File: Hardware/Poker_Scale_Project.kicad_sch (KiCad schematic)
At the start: 3 parts, among them U1 MCP6241-E/P

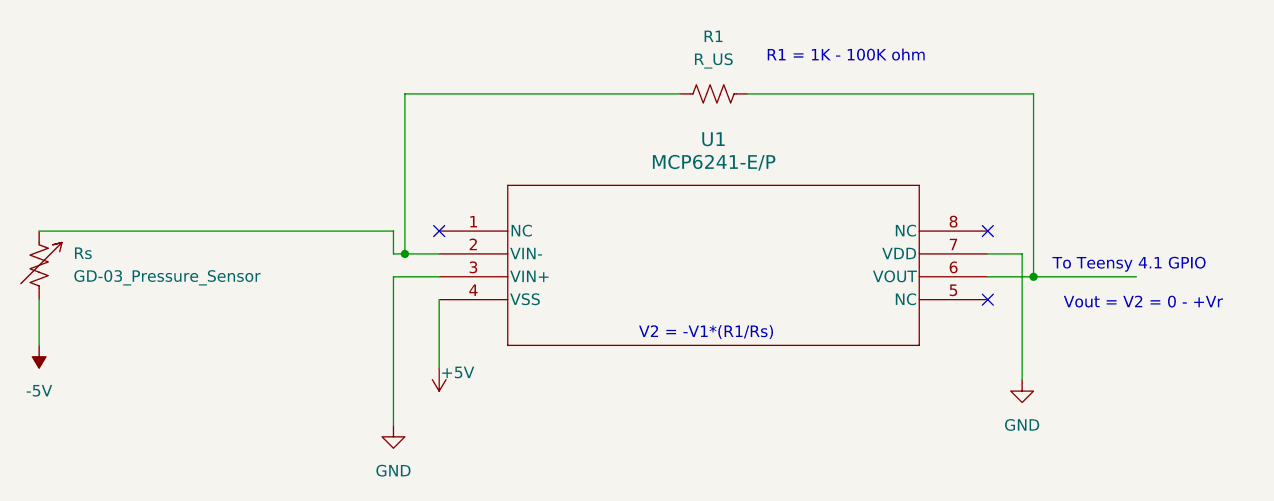
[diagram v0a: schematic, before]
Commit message: fixing Scale circuit, V2 = 0V - 3.3VDC
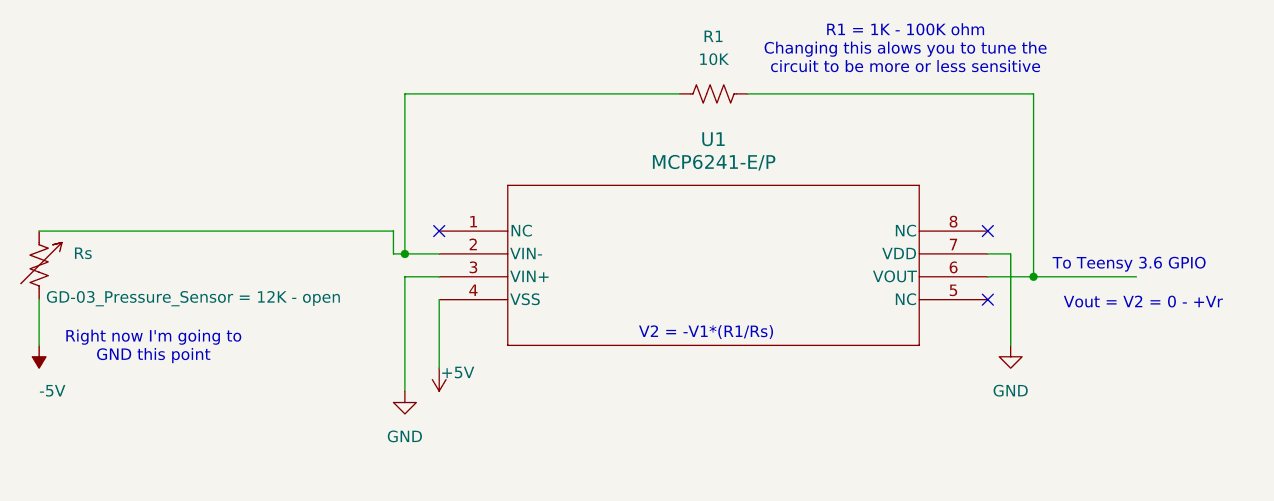
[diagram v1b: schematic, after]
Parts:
- R1: value R_US -> 10K
- Rs: value GD-03_Pressure_Sensor -> GD-03_Pressure_Sensor = 12K - open
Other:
- note added: "R1 = 1K - 100K ohm Changing this alows you to tune the circuit to be more or less sensitive"
- note added: "Right now I'm going to GND this point"
- note added: "To Teensy 3.6 GPIO"
- note removed: "R1 = 1K - 100K ohm"
- note removed: "To Teensy 4.1 GPIO"
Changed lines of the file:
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@@
 	(wire
 		(pts
-			(xy 167.64 101.6) (xy 163.83 101.6)
+			(xy 163.83 101.6) (xy 166.37 101.6)
 		)
 		(stroke
@@
 	(wire
 		(pts
-			(xy 102.87 104.14) (xy 97.79 104.14)
-		)
-		(stroke
-			(width 0)
-			(type default)
-		)
-	)
-	(wire
-		(pts
-			(xy 102.87 106.68) (xy 102.87 114.3)
+			(xy 102.87 114.3) (xy 102.87 106.68)
 		)
 		(stroke
@@
 	(wire
 		(pts
-			(xy 167.64 115.57) (xy 167.64 101.6)
+			(xy 99.06 104.14) (xy 102.87 104.14)
+		)
+		(stroke
+			(width 0)
+			(type default)
+		)
+	)
+	(wire
+		(pts
+			(xy 166.37 111.76) (xy 166.37 101.6)
 		)
 		(stroke
@@
 	(wire
 		(pts
+			(xy 99.06 116.84) (xy 99.06 104.14)
+		)
+		(stroke
+			(width 0)
+			(type default)
+		)
+	)
+	(wire
+		(pts
 			(xy 168.91 104.14) (xy 163.83 104.14)
 		)
@@
 		)
 	)
-	(wire
-		(pts
-			(xy 97.79 104.14) (xy 97.79 120.65)
-		)
-		(stroke
-			(width 0)
-			(type default)
+	(text "Right now I'm going to\nGND this point\n"
+		(exclude_from_sim no)
+		(at 71.12 112.014 0)
+		(effects
+			(font
+				(size 1.27 1.27)
+			)
 		)
 	)
@@
 		)
 	)
-	(text "To Teensy 4.1 GPIO\n"
+	(text "To Teensy 3.6 GPIO\n"
 		(exclude_from_sim no)
 		(at 179.578 102.87 0)
@@
 		)
 	)
-	(text "R1 = 1K - 100K ohm"
-		(exclude_from_sim no)
-		(at 148.082 79.756 0)
+	(text "R1 = 1K - 100K ohm\nChanging this alows you to tune the \ncircuit to be more or less sensitive "
+		(exclude_from_sim no)
+		(at 154.686 78.994 0)
 		(effects
 			(font
 				(size 1.27 1.27)
+			)
+		)
+	)
+	(symbol
+		(lib_id "power:GND")
+		(at 166.37 111.76 0)
+		(unit 1)
+		(exclude_from_sim no)
+		(in_bom yes)
+		(on_board yes)
+		(dnp no)
+		(fields_autoplaced yes)
+		(property "Reference" "#PWR03"
+			(at 166.37 118.11 0)
+			(effects
+				(font
+					(size 1.27 1.27)
+				)
+				(hide yes)
+			)
+		)
+		(property "Value" "GND"
+			(at 166.37 116.84 0)
+			(effects
+				(font
+					(size 1.27 1.27)
+				)
+			)
+		)
+		(property "Footprint" ""
+			(at 166.37 111.76 0)
+			(effects
+				(font
+					(size 1.27 1.27)
+				)
+				(hide yes)
+			)
+		)
+		(property "Datasheet" ""
+			(at 166.37 111.76 0)
+			(effects
+				(font
+					(size 1.27 1.27)
+				)
+				(hide yes)
+			)
+		)
+		(property "Description" "Power symbol creates a global label with name \"GND\" , ground"
+			(at 166.37 111.76 0)
+			(effects
+				(font
+					(size 1.27 1.27)
+				)
+				(hide yes)
+			)
+		)
+		(pin "1"
+		)
+		(instances
+			(project "Poker_Scale_Project"
+				(path "/dad62ed6-c118-47a2-9ae4-23cb6e0602fb"
+					(reference "#PWR03")
+					(unit 1)
+				)
 			)
 		)
@@
 		(on_board yes)
 		(dnp no)
-		(fields_autoplaced yes)
 		(property "Reference" "Rs"
 			(at 62.23 101.5618 0)
@@
 			)
 		)
-		(property "Value" "GD-03_Pressure_Sensor"
-			(at 62.23 104.1018 0)
+		(property "Value" "GD-03_Pressure_Sensor = 12K - open"
+			(at 59.182 106.426 0)
 			(effects
 				(font
@@
 	(symbol
 		(lib_id "power:GND")
-		(at 97.79 120.65 0)
-		(unit 1)
-		(exclude_from_sim no)
-		(in_bom yes)
-		(on_board yes)
-		(dnp no)
-		(fields_autoplaced yes)
-		(property "Reference" "#PWR01"
-			(at 97.79 127 0)
-			(effects
-				(font
-					(size 1.27 1.27)
-				)
-				(hide yes)
-			)
-		)
-		(property "Value" "GND"
-			(at 97.79 125.73 0)
-			(effects
-				(font
-					(size 1.27 1.27)
-				)
-			)
-		)
-		(property "Footprint" ""
-			(at 97.79 120.65 0)
-			(effects
-				(font
-					(size 1.27 1.27)
-				)
-				(hide yes)
-			)
-		)
-		(property "Datasheet" ""
-			(at 97.79 120.65 0)
-			(effects
-				(font
-					(size 1.27 1.27)
-				)
-				(hide yes)
-			)
-		)
-		(property "Description" "Power symbol creates a global label with name \"GND\" , ground"
-			(at 97.79 120.65 0)
-			(effects
-				(font
-					(size 1.27 1.27)
-				)
-				(hide yes)
-			)
-		)
-		(pin "1"
-		)
-		(instances
-			(project ""
-				(path "/dad62ed6-c118-47a2-9ae4-23cb6e0602fb"
-					(reference "#PWR01")
-					(unit 1)
-				)
-			)
-		)
-	)
-	(symbol
-		(lib_id "power:GND")
-		(at 167.64 115.57 0)
+		(at 99.06 116.84 0)
 		(unit 1)
 		(exclude_from_sim no)
@@
 		(fields_autoplaced yes)
 		(property "Reference" "#PWR02"
-			(at 167.64 121.92 0)
+			(at 99.06 123.19 0)
 			(effects
 				(font
@@
 		)
 		(property "Value" "GND"
-			(at 167.64 120.65 0)
+			(at 99.06 121.92 0)
 			(effects
 				(font
@@
 		)
 		(property "Footprint" ""
-			(at 167.64 115.57 0)
+			(at 99.06 116.84 0)
 			(effects
 				(font
@@
 		)
 		(property "Datasheet" ""
-			(at 167.64 115.57 0)
+			(at 99.06 116.84 0)
 			(effects
 				(font
@@
 		)
 		(property "Description" "Power symbol creates a global label with name \"GND\" , ground"
-			(at 167.64 115.57 0)
+			(at 99.06 116.84 0)
 			(effects
 				(font
@@
 			)
 		)
-		(property "Value" "R_US"
+		(property "Value" "10K"
 			(at 133.35 80.01 90)
 			(effects
@@
 	)
 	(symbol
+		(lib_id "power:+5V")
+		(at 102.87 114.3 180)
+		(unit 1)
+		(exclude_from_sim no)
+		(in_bom yes)
+		(on_board yes)
+		(dnp no)
+		(property "Reference" "#PWR01"
+			(at 102.87 110.49 0)
+			(effects
+				(font
+					(size 1.27 1.27)
+				)
+				(hide yes)
+			)
+		)
+		(property "Value" "+5V"
+			(at 104.902 114.808 0)
+			(effects
+				(font
+					(size 1.27 1.27)
+				)
+			)
+		)
+		(property "Footprint" ""
+			(at 102.87 114.3 0)
+			(effects
+				(font
+					(size 1.27 1.27)
+				)
+				(hide yes)
+			)
+		)
+		(property "Datasheet" ""
+			(at 102.87 114.3 0)
+			(effects
+				(font
+					(size 1.27 1.27)
+				)
+				(hide yes)
+			)
+		)
+		(property "Description" "Power symbol creates a global label with name \"+5V\""
+			(at 102.87 114.3 0)
+			(effects
+				(font
+					(size 1.27 1.27)
+				)
+				(hide yes)
+			)
+		)
+		(pin "1"
+		)
+		(instances
+			(project "Poker_Scale_Project"
+				(path "/dad62ed6-c118-47a2-9ae4-23cb6e0602fb"
+					(reference "#PWR01")
+					(unit 1)
+				)
+			)
+		)
+	)
+	(symbol
 		(lib_id "power:-5V")
 		(at 58.42 111.76 180)
@@
 		(on_board yes)
 		(dnp no)
-		(fields_autoplaced yes)
 		(property "Reference" "#PWR04"
 			(at 58.42 107.95 0)
@@
 					(size 1.27 1.27)
 				)
+				(justify right)
 			)
 		)
@@
 					(unit 1)
 				)
-			)
-		)
-	)
-	(symbol
-		(lib_id "power:+5V")
-		(at 102.87 114.3 180)
-		(unit 1)
-		(exclude_from_sim no)
-		(in_bom yes)
-		(on_board yes)
-		(dnp no)
-		(property "Reference" "#PWR03"
-			(at 102.87 110.49 0)
-			(effects
-				(font
-					(size 1.27 1.27)
-				)
-				(hide yes)
-			)
-		)
-		(property "Value" "+5V"
-			(at 104.902 114.808 0)
-			(effects
-				(font
-					(size 1.27 1.27)
-				)
-			)
-		)
-		(property "Footprint" ""
-			(at 102.87 114.3 0)
-			(effects
-				(font
-					(size 1.27 1.27)
-				)
-				(hide yes)
-			)
-		)
-		(property "Datasheet" ""
-			(at 102.87 114.3 0)
-			(effects
-				(font
-					(size 1.27 1.27)
-				)
-				(hide yes)
-			)
-		)
-		(property "Description" "Power symbol creates a global label with name \"+5V\""
-			(at 102.87 114.3 0)
-			(effects
-				(font
-					(size 1.27 1.27)
-				)
-				(hide yes)
-			)
-		)
-		(pin "1"
-		)
-		(instances
-			(project ""
-				(path "/dad62ed6-c118-47a2-9ae4-23cb6e0602fb"
-					(reference "#PWR03")
-					(unit 1)
-				)
